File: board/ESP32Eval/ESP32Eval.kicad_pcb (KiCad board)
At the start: 2 copper layers, 40 x 50 mm, 31 parts, among them J1 USB_B_Mini, J2 Conn_01x15, J3 Conn_01x15, Q1 Q_NPN_BCE, Q2 Q_NPN_BCE, SW1 SW_Push, SW2 SW_Push, U1 NCP1117-3.3_SOT223, U2 FT231XS, U3 ESP32-WROOM-32D

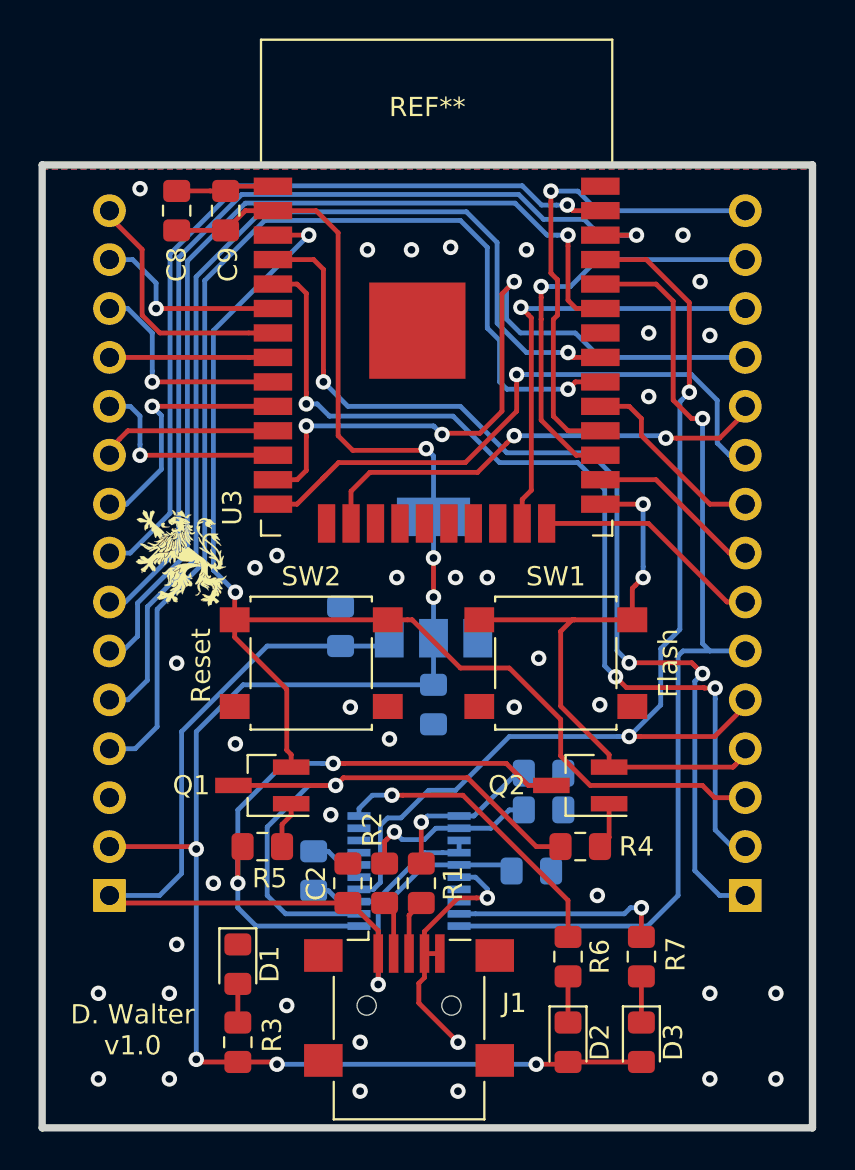
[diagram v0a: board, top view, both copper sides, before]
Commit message: Layout changes, added missing filter cap
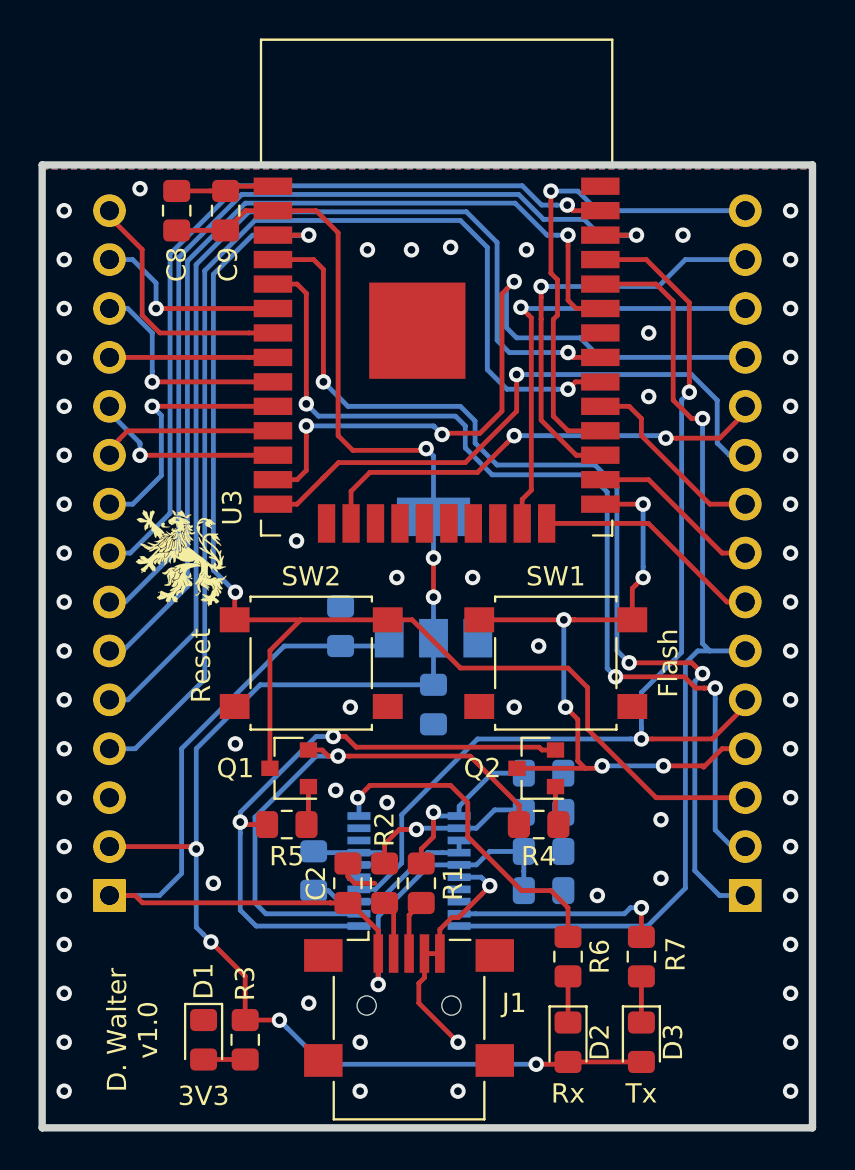
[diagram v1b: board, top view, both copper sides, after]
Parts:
- added C10: 4,7µF, Capacitor_SMD:C_0805_2012Metric_Pad1.15x1.40mm_HandSolder, B.Cu at (154.3, 121.7)
- C1, C4, C8: value C -> 10µF
- C2: value C -> 10nF
- C3, C5: value C -> 47pF
- C6, C7, C9: value C -> 100nF
- D2: value LED -> RX
- D3: value LED -> TX
- Q1, Q2: value Q_NPN_BCE -> BC817; footprint Package_TO_SOT_SMD:SOT-23_Handsoldering -> Package_TO_SOT_SMD:SOT-23
- R1, R2: value R -> 27R
- R3, R6, R7: value R -> 270R
- R4, R5: value R -> 10k
- SW1: value SW_Push -> SW_Flash
- SW2: value SW_Push -> SW_Reset
- moved D1 4.31 mm to (136.7, 129.4)
- moved Q2 2.45 mm to (153.9, 115.3)
- moved R4 2.44 mm to (154.1, 118.2)
- moved R5 1.71 mm to (141.0, 118.2)
- moved Q1 1.66 mm to (141.1, 115.3)
- moved C6 1.20 mm to (154.3, 119.6)
- moved R3 0.40 mm to (138.8, 129.4), turned to 90 degrees
- moved C5 0.13 mm to (154.3, 117.6)
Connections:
- Q1 pad 2: Net-(J2-Pad3) -> Net-(Q1-Pad2)
- Q1 pad 3: Net-(Q1-Pad3) -> Net-(J2-Pad3)
- Q2 pad 2: Net-(J2-Pad4) -> Net-(Q2-Pad2)
- Q2 pad 3: Net-(Q2-Pad3) -> Net-(J2-Pad4)
- R4 pad 2: Net-(Q1-Pad3) -> Net-(Q1-Pad2)
- R5 pad 2: Net-(Q2-Pad3) -> Net-(Q2-Pad2)
- U2 pad 1: Net-(Q2-Pad3) -> Net-(Q2-Pad2)
- U2 pad 2: Net-(Q1-Pad3) -> Net-(Q1-Pad2)
- U2 pad 7: Net-(U2-Pad7) -> GND
- U2 pad 9: Net-(U2-Pad9) -> GND
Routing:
- net Net-(Q1-Pad3): track 31.8 -> 0.00 mm, vias 1 -> 0
- net Net-(Q2-Pad3): track 31.5 -> 0.00 mm, vias 2 -> 0
- net Net-(Q2-Pad2): track 0.00 -> 31.3 mm, vias 0 -> 2
- net Net-(Q1-Pad2): track 0.00 -> 28.9 mm, vias 0 -> 1
- net Net-(J2-Pad4): track 33.8 -> 37.9 mm, vias 2 -> 6
- net GND: track 21.4 -> 25.3 mm, vias 39 -> 64
- net +3V3: track 95.7 -> 92.5 mm
- net +5V: track 54.4 -> 56.5 mm
- net Net-(R6-Pad2): track 15.7 -> 17.4 mm
- net Net-(J2-Pad3): track 65.0 -> 66.4 mm
- net Net-(J3-Pad5): track 52.7 -> 53.6 mm
- net Net-(J3-Pad11): track 11.0 -> 10.2 mm
- net Net-(J2-Pad2): track 50.0 -> 50.7 mm
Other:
- board text added: "3V3"
- board text added: "Rx"
- board text added: "Tx"

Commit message: Connected USB Shield trough Capacitors
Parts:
- added C11: 10nF, Capacitor_SMD:C_0805_2012Metric_Pad1.15x1.40mm_HandSolder, F.Cu at (140.8, 127.9)
- added C12: 10nF, Capacitor_SMD:C_0805_2012Metric_Pad1.15x1.40mm_HandSolder, F.Cu at (154.0, 127.9)
- moved D1 3.05 mm to (133.6, 129.4)
- moved R3 2.92 mm to (135.9, 129.4)
- moved R6 2.43 mm to (158.0, 125.3)
- moved R7 2.43 mm to (161.8, 125.3)
- moved D2 2.41 mm to (158.0, 129.5)
- moved D3 2.41 mm to (161.8, 129.5)
- moved G*** 1.05 mm to (135.8, 103.4)
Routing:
- net Net-(C11-Pad1): track 0.00 -> 22.6 mm
- net GND: track 25.3 -> 38.4 mm, vias 64 -> 67
- net +3V3: track 92.5 -> 101.8 mm, vias 7 -> 6
- net Net-(R7-Pad2): track 11.1 -> 12.7 mm
- net Net-(R6-Pad2): track 17.4 -> 18.8 mm
- net (no net): vias 1 -> 0
